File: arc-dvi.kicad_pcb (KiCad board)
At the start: 4 copper layers, 94.6 x 71.1 mm, 133 parts, among them J1 Conn_01x24_MountingPin, J2 VIDC Interposer, J3 SWD, J4 BOOT, J5 USB_B_Micro, J6 PWR, Q1 Q_NPN_BCE, U1 W25Q32JVSS, U2 RP2040, U3 ICE40HX4K-TQ144, U4 TDA19988BHN/C1,557, U5 LT1963AxST-3.3, U6 TLV70012_SOT23-5, U7 TLV70018_SOT23-5, Y1 12M 18pF

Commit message: v2: ADV7513 and FFC
Large work much progress - almost routed
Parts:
- removed FB6: FerriteBead_Small, Inductor_SMD:L_0603_1608Metric
- added C58: 0.1u, Capacitor_SMD:C_0603_1608Metric, F.Cu at (123.0, 93.0)
- added C59: 0.1u, Capacitor_SMD:C_0603_1608Metric, B.Cu at (124.8, 85.5)
- added D2: ESDA6V1BC6, Package_TO_SOT_SMD:SOT-23-6, F.Cu at (130.2, 67.2)
- added D3: D, Diode_SMD:D_0603_1608Metric, F.Cu at (124.0, 78.5)
- added D4: RCLAMP3328P, Package_DFN_QFN:UDFN-9_1.0x3.8mm_P0.5mm, F.Cu at (122.2, 70.8)
- added F1: 50mA, Fuse:Fuse_1206_3216Metric_Pad1.42x1.75mm_HandSolder, F.Cu at (131.2, 61.0)
- added J7: Misc, Connector_PinHeader_2.00mm:PinHeader_2x04_P2.00mm_Vertical, F.Cu at (74.0, 59.1)
- added J8: HDMI_A, Connector_HDMI:HDMI_A_Molex_208658-1001_Horizontal, F.Cu at (118.8, 57.0)
- added R18: 2K, Resistor_SMD:R_0603_1608Metric, B.Cu at (132.0, 76.5)
- added R19: 2K, Resistor_SMD:R_0603_1608Metric, B.Cu at (110.5, 73.8)
- added R20: 27K, Resistor_SMD:R_0603_1608Metric, F.Cu at (121.0, 77.8)
- added R21: 22, Resistor_SMD:R_0603_1608Metric, F.Cu at (110.8, 82.8)
- C34, C36, C37, C53, U5: moved to F.Cu
- C42: value 1u -> 10u
- C44: value 10u -> 0.1u; footprint Capacitor_SMD:C_0805_2012Metric -> Capacitor_SMD:C_0603_1608Metric
- C46: value 1u -> 0.1u
- C52: value 1u -> 0.1u; moved to F.Cu
- J1: value Conn_01x24_MountingPin -> Connector_50pin_FFC; footprint Connector_FFC-FPC:TE_2-1734839-4_1x24-1MP_P0.5mm_Horizontal -> Connector_FFC-FPC:Hirose_FH12-50S-0.5SH_1x50-1MP_P0.50mm_Horizontal
- J2: value VIDC Interposer -> 5V_IN; footprint Connector_PinHeader_2.54mm:PinHeader_2x25_P2.54mm_Vertical -> Connector_PinHeader_2.54mm:PinHeader_1x02_P2.54mm_Horizontal
- J6: value PWR -> PWR_USB; footprint Connector_PinHeader_2.54mm:PinHeader_1x03_P2.54mm_Vertical -> Connector_PinHeader_2.54mm:PinHeader_1x02_P2.54mm_Vertical
- R12, R13: value 10K -> 2K
- R14: value 10K, 1% -> 887, 1%
- R16: value 4k7 -> 4K7
- TP5: value AP4 -> SPD
- TP6: value AP3 -> P50
- TP7: value AP2 -> MCLK
- U4: value TDA19988BHN/C1,557 -> ADV7513BSWZ; footprint matt:QFN50P900X900X100-65N -> matt:QFP50P1200X1200X160-65N
- moved J1 80.9 mm to (80.0, 122.0), turned to 0 degrees
- moved TP1 80.2 mm to (56.2, 77.5)
- moved TP6 46.9 mm to (96.0, 119.2)
- moved C46 41.4 mm to (134.8, 79.5), turned to 90 degrees
- moved J4 39.3 mm to (71.5, 53.5)
- moved C34 37.6 mm to (56.8, 95.8), turned to 180 degrees
- moved FB1 31.8 mm to (61.8, 97.0), turned to -90 degrees
- moved C56 31.3 mm to (123.8, 79.3), turned to -90 degrees
- moved C42 30.6 mm to (136.8, 80.8), turned to 0 degrees
- moved C35 30.6 mm to (56.3, 86.7)
- moved C43 29.2 mm to (136.8, 82.8), turned to 0 degrees
- moved RN2 28.3 mm to (114.8, 88.8)
- moved TP7 28.3 mm to (139.5, 90.5)
- moved R14 27.7 mm to (140.5, 83.5), turned to 0 degrees
- moved RN1 27.4 mm to (114.8, 85.0)
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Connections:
- C42 pad 1: /Video/VDDA -> /Video/AVDD
- C43 pad 1: /Video/VDDA -> /Video/AVDD
- C44 pad 1: +1V8 -> /Video/AVDD
- C45 pad 1: /Video/VDDA_TX -> /Video/PVDD
- C46 pad 1: +1V8 -> /Video/AVDD
- C47 pad 1: /Video/VDDA_TX -> /Video/PVDD
- C48 pad 1: /Video/VDDA_PLL -> /Video/DVDD
- C50 pad 1: /Video/VDDA_PLL -> /Video/DVDD
- C52 pad 1: /Video/VDD_CORE -> /Video/PVDD
- C53 pad 1: /Video/VDD_CORE -> /Video/DVDD
- C54 pad 1: /Video/VDD_IO -> /Video/DVDD3
- C56 pad 1: /Video/VDD_IO -> /Video/DVDD3
- FB1 pad 2: /HOST_5V -> Net-(FB1-Pad2)
- FB3 pad 2: /Video/VDDA -> /Video/AVDD
- FB4 pad 2: /Video/VDDA_TX -> /Video/PVDD
- FB5 pad 2: /Video/VDDA_PLL -> /Video/DVDD
- FB7 pad 1: +1V8 -> +3V3
- FB7 pad 2: /Video/VDD_IO -> /Video/DVDD3
- J1 pad 1: VID_HPD -> VD0
- J1 pad 10: VID_CK+ -> VD8
- J1 pad 11: VID_D0- -> VD9
- J1 pad 12: GND -> VD10
- J1 pad 13: VID_D0+ -> VD11
- J1 pad 14: VID_D1- -> VD12
- J1 pad 15: GND -> VD13
- J1 pad 16: VID_D1+ -> GND
- J1 pad 17: VID_D2- -> VD14
- J1 pad 18: GND -> VD15
- J1 pad 19: VID_D2+ -> VD16
- J1 pad 2: +5V -> VD1
- J1 pad 20: CFG_SW3 -> VD17
- J1 pad 21: CFG_SW2 -> VD18
- J1 pad 22: CFG_SW1 -> VD19
- J1 pad 23: MCU_A2 -> VD20
- J1 pad 24: MCU_A1 -> GND
- J1 pad 3: GND -> VD2
- J1 pad 4: VID_DISP_SDA -> VD3
- J1 pad 5: VID_DISP_SCL -> VD4
- J1 pad 6: CFG_SW4 -> VD5
- J1 pad 7: VID_CEC -> VD6
- J1 pad 8: VID_CK- -> GND
- J1 pad 9: GND -> VD7
- J2 pad 1: VD15 -> Net-(FB1-Pad2)
- J2 pad 2: VD14 -> GND
- J6 pad 1: /VBUS -> +5V
- J6 pad 2: +5V -> /VBUS
- R12 pad 2: VID_DISP_SDA -> /Video/DDC_SDA
- R13 pad 2: VID_DISP_SCL -> /Video/DDC_SCL
- RN1 pad 1: RGB8 -> RGB23
- RN1 pad 2: RGB23 -> RGB22
- RN1 pad 3: RGB22 -> RGB21
- RN1 pad 4: RGB21 -> RGB20
- RN13 pad 1: ALT_VID_I2S_CLK -> ALT_VID_I2S_DATA
- RN13 pad 2: ALT_VID_I2S_WS -> ALT_VID_I2S_CLK
- RN13 pad 3: ALT_VID_I2S_DATA -> ALT_VID_I2S_WS
- RN13 pad 6: Net-(RN12-Pad8) -> Net-(RN12-Pad6)
- RN13 pad 7: Net-(RN12-Pad6) -> Net-(RN12-Pad7)
- RN13 pad 8: Net-(RN12-Pad7) -> Net-(RN12-Pad8)
- RN2 pad 1: RGB20 -> RGB19
- RN2 pad 2: RGB19 -> RGB18
- RN2 pad 3: RGB18 -> RGB17
- RN2 pad 4: RGB17 -> RGB16
- RN3 pad 1: VID_OUT_PCLK -> RGB11
- RN3 pad 2: RGB11 -> RGB10
- RN3 pad 3: RGB10 -> RGB9
- RN3 pad 4: RGB9 -> VID_OUT_PCLK
- RN3 pad 8: /Video/PCLK_R -> Net-(RN3-Pad8)
- RN4 pad 1: RGB16 -> RGB0
- RN4 pad 3: VID_OUT_VS -> VID_OUT_HS
- RN4 pad 4: VID_OUT_HS -> VID_OUT_VS
- RN4 pad 5: Net-(RN4-Pad5) -> Net-(U4-Pad2)
- RN4 pad 6: Net-(RN4-Pad6) -> Net-(U4-Pad64)
- RN4 pad 7: Net-(RN4-Pad7) -> Net-(U4-Pad63)
- RN4 pad 8: Net-(RN4-Pad8) -> Net-(U4-Pad62)
- RN5 pad 1: RGB3 -> RGB4
- RN5 pad 2: RGB2 -> RGB3
- RN5 pad 3: RGB1 -> RGB2
- RN5 pad 4: RGB0 -> RGB1
- RN6 pad 1: RGB7 -> RGB8
- RN6 pad 2: RGB6 -> RGB7
- RN6 pad 3: RGB5 -> RGB6
- RN6 pad 4: RGB4 -> RGB5
- TP6 pad 1: Net-(TP6-Pad1) -> Net-(J1-Pad50)
- U2 pad 31: CFG_SW4 -> MCU_VID_SDA
- U2 pad 32: CFG_SW3 -> MCU_VID_SCL
- U2 pad 36: MCU_A1 -> /MCU/spare24
- U2 pad 37: MCU_A2 -> /MCU/spare25
- U2 pad 38: CFG_SW2 -> /MCU/spare26
- U2 pad 39: CFG_SW1 -> /MCU/spare27
- U2 pad 40: MCU_VID_SDA -> /MCU/spare28
- U2 pad 41: MCU_VID_SCL -> ID_DET
- U3 pad 1: VID_OUT_HS -> VID_OUT_VS
- U3 pad 10: RGB20 -> RGB4
- U3 pad 101: VD30 -> VD23
- U3 pad 102: VD31 -> VD24
- U3 pad 104: VD0 -> VD25
- U3 pad 105: VD1 -> VD26
- U3 pad 106: VD2 -> VD27
- U3 pad 107: VD3 -> VD28
- U3 pad 11: RGB21 -> RGB5
- U3 pad 110: VD4 -> VD29
- U3 pad 112: VD5 -> VD30
- U3 pad 113: VD6 -> VD31
- U3 pad 114: VD7 -> VnVIDW
- U3 pad 115: VD8 -> VnHS
- U3 pad 116: VD9 -> VnVCS
- U3 pad 117: VD10 -> VnVIDRQ
- U3 pad 118: VD11 -> VnSNDRQ
- U3 pad 119: VD12 -> VFLYBK
- U3 pad 12: RGB22 -> RGB6
- U3 pad 120: VD13 -> VCKIN
- U3 pad 121: VD14 -> VVIDAK
- U3 pad 122: VD15 -> VSNDAK
- U3 pad 142: ALT_VID_I2S_DATA -> ALT_VID_I2S_WS
- U3 pad 143: ALT_VID_I2S_WS -> ALT_VID_I2S_CLK
- U3 pad 144: ALT_VID_I2S_CLK -> ALT_VID_I2S_DATA
- U3 pad 15: RGB23 -> RGB7
- U3 pad 17: RGB9 -> VID_OUT_PCLK
- U3 pad 18: RGB10 -> RGB9
- U3 pad 19: RGB11 -> RGB10
- U3 pad 2: VID_OUT_VS -> VID_OUT_HS
- U3 pad 20: VID_OUT_PCLK -> RGB11
- U3 pad 25: RGB0 -> RGB16
- U3 pad 26: RGB1 -> RGB17
- U3 pad 28: RGB2 -> RGB18
- U3 pad 29: RGB3 -> RGB19
- U3 pad 31: RGB4 -> RGB20
- U3 pad 32: RGB5 -> RGB21
- U3 pad 33: RGB6 -> RGB22
- U3 pad 34: RGB7 -> RGB23
- U3 pad 38: unconnected-(U3-Pad38) -> VID_CEC_CLK
- U3 pad 4: RGB16 -> RGB0
- U3 pad 7: RGB17 -> RGB1
- U3 pad 73: VVIDAK -> VD0
- U3 pad 74: VSNDAK -> VD1
- U3 pad 75: VFLYBK -> VD2
- U3 pad 76: VnSNDRQ -> VD3
- U3 pad 78: VnVIDRQ -> VD4
- U3 pad 79: VnHS -> VD5
- U3 pad 8: RGB18 -> RGB2
- U3 pad 80: VnVCS -> VD6
- U3 pad 81: VnVIDW -> VD7
- U3 pad 82: VD16 -> VD8
- U3 pad 83: VD17 -> VD9
- U3 pad 84: VD18 -> VD10
- U3 pad 85: VD19 -> VD11
- U3 pad 87: VD20 -> VD12
- U3 pad 88: VD21 -> VD13
- U3 pad 9: RGB19 -> RGB3
- U3 pad 90: VD22 -> VD14
- U3 pad 91: VD23 -> VD15
- U3 pad 93: VCKIN -> VD16
- U3 pad 94: VD24 -> VD17
- U3 pad 95: VD25 -> VD18
- U3 pad 96: VD26 -> VD19
- U3 pad 97: VD27 -> VD20
- U3 pad 98: VD28 -> VD21
- U3 pad 99: VD29 -> VD22
- U4 pad 1: Net-(RN7-Pad7) -> /Video/DVDD
- U4 pad 10: Net-(RN1-Pad7) -> Net-(RN12-Pad6)
- U4 pad 11: Net-(RN1-Pad6) -> /Video/DVDD
- U4 pad 12: Net-(RN1-Pad5) -> /Video/PVDD
- U4 pad 13: Net-(RN2-Pad8) -> /Video/PVDD
- U4 pad 14: /Video/VDD_IO -> Net-(R14-Pad1)
- U4 pad 15: Net-(RN2-Pad7) -> /Video/AVDD
- U4 pad 16: Net-(RN2-Pad6) -> /Video/HPD
- U4 pad 17: Net-(RN2-Pad5) -> /Video/TXC-
- U4 pad 18: Net-(RN4-Pad8) -> /Video/TXC+
- U4 pad 19: GND -> /Video/AVDD
- U4 pad 2: Net-(RN7-Pad6) -> Net-(U4-Pad2)
- U4 pad 20: Net-(RN4-Pad7) -> /Video/TX0-
- U4 pad 21: Net-(RN4-Pad6) -> /Video/TX0+
- U4 pad 22: Net-(RN4-Pad5) -> Net-(R18-Pad1)
- U4 pad 23: Net-(RN12-Pad7) -> /Video/TX1-
- U4 pad 24: Net-(RN12-Pad6) -> /Video/TX1+
- U4 pad 25: Net-(RN12-Pad8) -> /Video/AVDD
- U4 pad 26: Net-(TP7-Pad1) -> /Video/TX2-
- U4 pad 27: Net-(TP6-Pad1) -> /Video/TX2+
- U4 pad 28: Net-(TP5-Pad1) -> MCU_VID_IRQ
- U4 pad 29: /Video/VDD_CORE -> /Video/DVDD3
- U4 pad 3: Net-(RN7-Pad5) -> Net-(TP5-Pad1)
- U4 pad 30: VID_CEC -> /Video/CEC
- U4 pad 31: VID_HPD -> /Video/DVDD
- U4 pad 32: VID_DISP_SDA -> Net-(U4-Pad32)
- U4 pad 33: VID_DISP_SCL -> /Video/DDC_SCL
- U4 pad 34: Net-(R14-Pad1) -> /Video/DDC_SDA
- U4 pad 35: /Video/VDDA -> MCU_VID_SCL
- U4 pad 36: /Video/VDDA_TX -> MCU_VID_SDA
- U4 pad 37: VID_CK- -> Net-(RN1-Pad8)
- U4 pad 38: VID_CK+ -> Net-(RN1-Pad7)
- U4 pad 39: VID_D0- -> Net-(RN1-Pad6)
- U4 pad 4: /Video/PCLK_R -> Net-(TP7-Pad1)
- U4 pad 40: VID_D0+ -> Net-(RN1-Pad5)
- U4 pad 41: /Video/VDDA_TX -> Net-(RN2-Pad8)
- U4 pad 42: VID_D1- -> Net-(RN2-Pad7)
- U4 pad 43: VID_D1+ -> Net-(RN2-Pad6)
- U4 pad 44: VID_D2- -> Net-(RN2-Pad5)
- U4 pad 45: VID_D2+ -> Net-(RN7-Pad8)
- U4 pad 46: /Video/VDDA_TX -> Net-(RN7-Pad7)
- U4 pad 47: /Video/VDDA_PLL -> Net-(RN7-Pad6)
- U4 pad 48: /Video/VDDA_PLL -> Net-(RN7-Pad5)
- U4 pad 49: GND -> Net-(RN3-Pad8)
- U4 pad 5: /Video/VDD_CORE -> Net-(RN12-Pad8)
- U4 pad 50: MCU_VID_IRQ -> Net-(RN3-Pad7)
- U4 pad 51: MCU_VID_SDA -> /Video/DVDD
- U4 pad 52: MCU_VID_SCL -> Net-(RN3-Pad6)
- U4 pad 53: GND -> Net-(RN3-Pad5)
- U4 pad 54: GND -> Net-(RN6-Pad8)
- U4 pad 55: /Video/VDD_IO -> Net-(RN6-Pad7)
- U4 pad 56: Net-(RN6-Pad8) -> Net-(RN6-Pad6)
- U4 pad 57: Net-(RN6-Pad7) -> Net-(RN6-Pad5)
- U4 pad 58: Net-(RN6-Pad6) -> Net-(RN5-Pad8)
- U4 pad 59: Net-(RN6-Pad5) -> Net-(RN5-Pad7)
- U4 pad 6: Net-(RN3-Pad7) -> unconnected-(U4-Pad6)
- U4 pad 60: Net-(RN5-Pad8) -> Net-(RN5-Pad6)
- U4 pad 61: Net-(RN5-Pad7) -> Net-(RN5-Pad5)
- U4 pad 62: Net-(RN5-Pad6) -> Net-(U4-Pad62)
- U4 pad 63: Net-(RN5-Pad5) -> Net-(U4-Pad63)
- U4 pad 64: Net-(RN7-Pad8) -> Net-(U4-Pad64)
- U4 pad 7: Net-(RN3-Pad6) -> unconnected-(U4-Pad7)
- U4 pad 8: Net-(RN3-Pad5) -> unconnected-(U4-Pad8)
- U4 pad 9: Net-(RN1-Pad8) -> Net-(RN12-Pad7)
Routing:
- net GND: track 834.2 -> 566.2 mm, vias 85 -> 56
- net +5V: track 225.1 -> 47.8 mm
- net ID_DET: track 0.00 -> 94.3 mm, vias 0 -> 4
- net VID_CEC: track 76.9 -> 0.00 mm, vias 2 -> 0
- net VID_HPD: track 68.1 -> 0.00 mm
- net VID_DISP_SDA: track 64.7 -> 0.00 mm, vias 1 -> 0
- net VID_DISP_SCL: track 61.9 -> 0.00 mm, vias 1 -> 0
- net /Video/DVDD: track 0.00 -> 60.8 mm, vias 0 -> 4
- net VID_CK-: track 54.3 -> 0.00 mm
- net VID_CK+: track 54.3 -> 0.00 mm
- net VID_D0-: track 54.2 -> 0.00 mm
- net VID_D0+: track 54.2 -> 0.00 mm
- net VID_D2-: track 54.2 -> 0.00 mm
- net VID_D2+: track 54.2 -> 0.00 mm
- net VID_D1+: track 54.1 -> 0.00 mm
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- removed copper zone on In1.Cu, net +3V3
- removed copper zone on In2.Cu, net GND
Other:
- board size 94.6 x 71.1 mm -> 100 x 77 mm
- board text added: "Caution! Polarity! Check 3 times!"
- board text added: "Check values of C58 and friends, equal spread pls"
- board text added: "Gnd 5V"
- board text added: "USB boot ___"
- board text added: "___ Reset"
- board text added: "v2.0 190523 (c) 2023 Matt Evans"
- board text removed: "5"
- board text removed: "5B"
- board text removed: ">Reset"
- board text removed: ">USB boot"
- board text removed: "Digital out"
- board text removed: "^Pin 1"
- board text removed: "v1.0 180622 (c) 2022 Matt Evans"

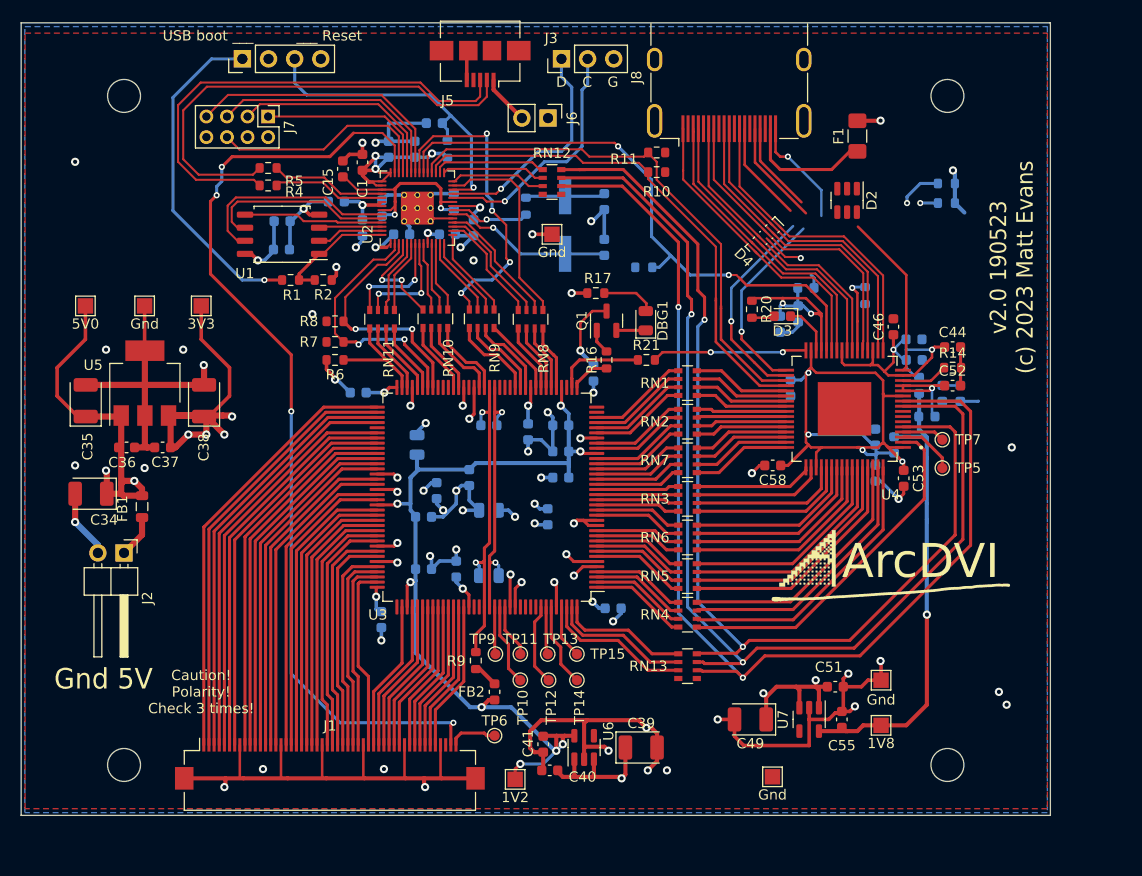
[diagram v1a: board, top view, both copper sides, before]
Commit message: 2.0 candiate: routed, looks neat, passes DRC
DVI differential pairs aren't tuned that nicely, but 'probs ok'
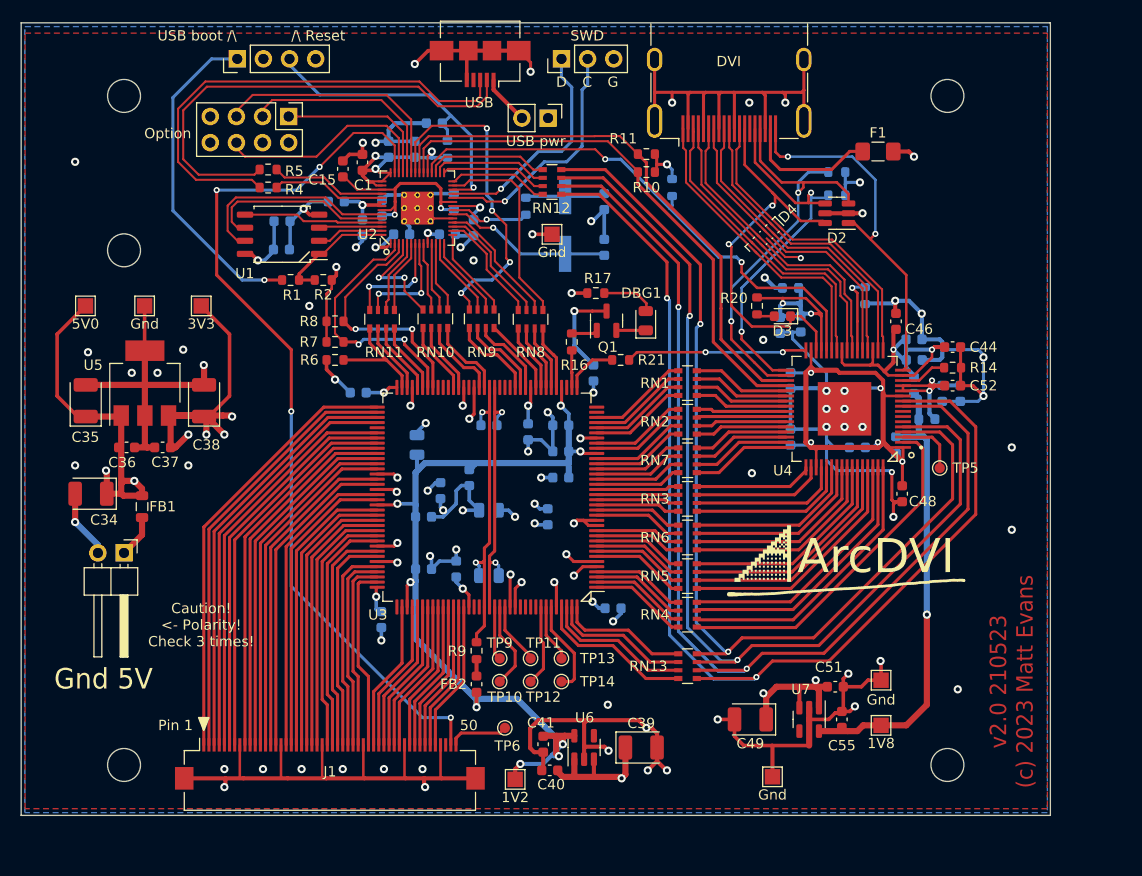
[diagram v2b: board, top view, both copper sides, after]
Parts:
- removed TP15: 219, TestPoint:TestPoint_Pad_D1.0mm
- removed TP7: MCLK, TestPoint:TestPoint_Pad_D1.0mm
- added H5: MountingHole, MountingHole:MountingHole_3.2mm_M3, F.Cu at (60.0, 72.1)
- C48: moved to F.Cu
- C53, C58: moved to B.Cu
- J7: footprint Connector_PinHeader_2.00mm:PinHeader_2x04_P2.00mm_Vertical -> Connector_PinHeader_2.54mm:PinHeader_2x04_P2.54mm_Vertical
- moved R12 11.1 mm to (129.2, 64.5)
- moved R13 10.7 mm to (129.2, 66.8)
- moved C53 8.84 mm to (132.0, 86.2)
- moved R19 8.22 mm to (113.2, 66.0), turned to -90 degrees
- moved C48 6.08 mm to (135.6, 95.8), turned to -90 degrees
- moved G*** 4.36 mm to (132.2, 103.2)
- moved R16 3.81 mm to (103.5, 81.0)
- moved C58 3.25 mm to (124.8, 90.2), turned to 90 degrees
- moved C50 3.05 mm to (131.2, 91.2), turned to 180 degrees
- moved F1 2.50 mm to (133.2, 62.5), turned to 0 degrees
- moved R21 2.50 mm to (108.2, 82.8)
- moved C54 2.08 mm to (123.8, 79.4)
- moved TP10 2.00 mm to (96.5, 114.0)
- moved C56 2.00 mm to (125.8, 79.2)
- moved J7 2.00 mm to (76.0, 59.1)
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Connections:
- D2 pad 3: /Video/DDC_SCL -> /Video/DDC_SDA
- D2 pad 4: /Video/DDC_SDA -> /Video/DDC_SCL
- J7 pad 7: /MCU/spare24 -> unconnected-(J7-Pad7)
- RN12 pad 1: VID_I2S_DATA -> VID_I2S_MCLK
- RN12 pad 2: VID_I2S_CLK -> VID_I2S_DATA
- RN12 pad 3: VID_I2S_WS -> VID_I2S_CLK
- RN12 pad 4: unconnected-(RN12-Pad4) -> VID_I2S_WS
- RN12 pad 5: unconnected-(RN12-Pad5) -> Net-(RN12-Pad5)
- RN13 pad 1: ALT_VID_I2S_DATA -> ALT_VID_I2S_MCLK
- RN13 pad 2: ALT_VID_I2S_CLK -> ALT_VID_I2S_DATA
- RN13 pad 3: ALT_VID_I2S_WS -> ALT_VID_I2S_CLK
- RN13 pad 4: unconnected-(RN13-Pad4) -> ALT_VID_I2S_WS
- RN13 pad 5: unconnected-(RN13-Pad5) -> Net-(RN12-Pad5)
- U2 pad 31: MCU_VID_SDA -> VID_I2S_MCLK
- U2 pad 32: MCU_VID_SCL -> MCU_VID_IRQ
- U2 pad 34: MCU_VID_IRQ -> MCU_VID_SDA
- U2 pad 35: FPGA_CLK -> MCU_VID_SCL
- U2 pad 36: /MCU/spare24 -> FPGA_CLK
- U3 pad 141: Net-(TP15-Pad1) -> ALT_VID_I2S_WS
- U3 pad 142: ALT_VID_I2S_WS -> ALT_VID_I2S_CLK
- U3 pad 143: ALT_VID_I2S_CLK -> ALT_VID_I2S_DATA
- U3 pad 144: ALT_VID_I2S_DATA -> ALT_VID_I2S_MCLK
- U3 pad 37: /FPGA/DBG_LED -> VID_CEC_CLK
- U3 pad 38: VID_CEC_CLK -> /FPGA/DBG_LED
- U4 pad 10: Net-(RN12-Pad6) -> Net-(RN12-Pad5)
- U4 pad 4: Net-(TP7-Pad1) -> Net-(RN12-Pad8)
- U4 pad 5: Net-(RN12-Pad8) -> Net-(RN12-Pad7)
- U4 pad 9: Net-(RN12-Pad7) -> Net-(RN12-Pad6)
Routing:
- net GND: track 566.2 -> 939.3 mm, vias 56 -> 81
- net +5V: track 47.8 -> 167.1 mm
- net Net-(RN12-Pad5): track 0.00 -> 109.9 mm, vias 0 -> 2
- net +3V3: track 404.1 -> 481.4 mm
- net /MCU/spare24: track 26.8 -> 0.00 mm
- net /Video/CEC: track 14.7 -> 39.4 mm, vias 0 -> 2
- net +1V1: track 0.00 -> 20.4 mm, vias 0 -> 2
- net ALT_VID_I2S_MCLK: track 0.00 -> 12.6 mm
- net /Video/DDC_SDA: track 30.8 -> 43.2 mm
- net VID_I2S_MCLK: track 0.00 -> 12.0 mm
- net /Video/HPD: track 26.8 -> 36.1 mm, vias 1 -> 2
- net /Video/DVDD: track 60.8 -> 52.3 mm, vias 4 -> 5
- net ID_DET: track 94.3 -> 87.7 mm
- net MCU_VID_IRQ: track 58.1 -> 52.0 mm
- net Net-(RN12-Pad7): track 107.4 -> 101.9 mm
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- added copper zone on In2.Cu, net +3V3
- added copper zone on In1.Cu, net GND
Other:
- board text added: "/\ Reset"
- board text added: "50"
- board text added: "Caution! <- Polarity! Check 3 times!"
- board text added: "DVI"
- board text added: "Option"
- board text added: "Pin 1"
- board text added: "SWD"
- board text added: "USB"
- board text added: "USB boot /\"
- board text added: "USB pwr"
- board text added: "v2.0 210523 (c) 2023 Matt Evans"
- board text removed: "Caution! Polarity! Check 3 times!"
- board text removed: "Check values of C58 and friends, equal spread pls"
- board text removed: "USB boot ___"
- board text removed: "___ Reset"
- board text removed: "v2.0 190523 (c) 2023 Matt Evans"

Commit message: Tuned pairs (better, at least)
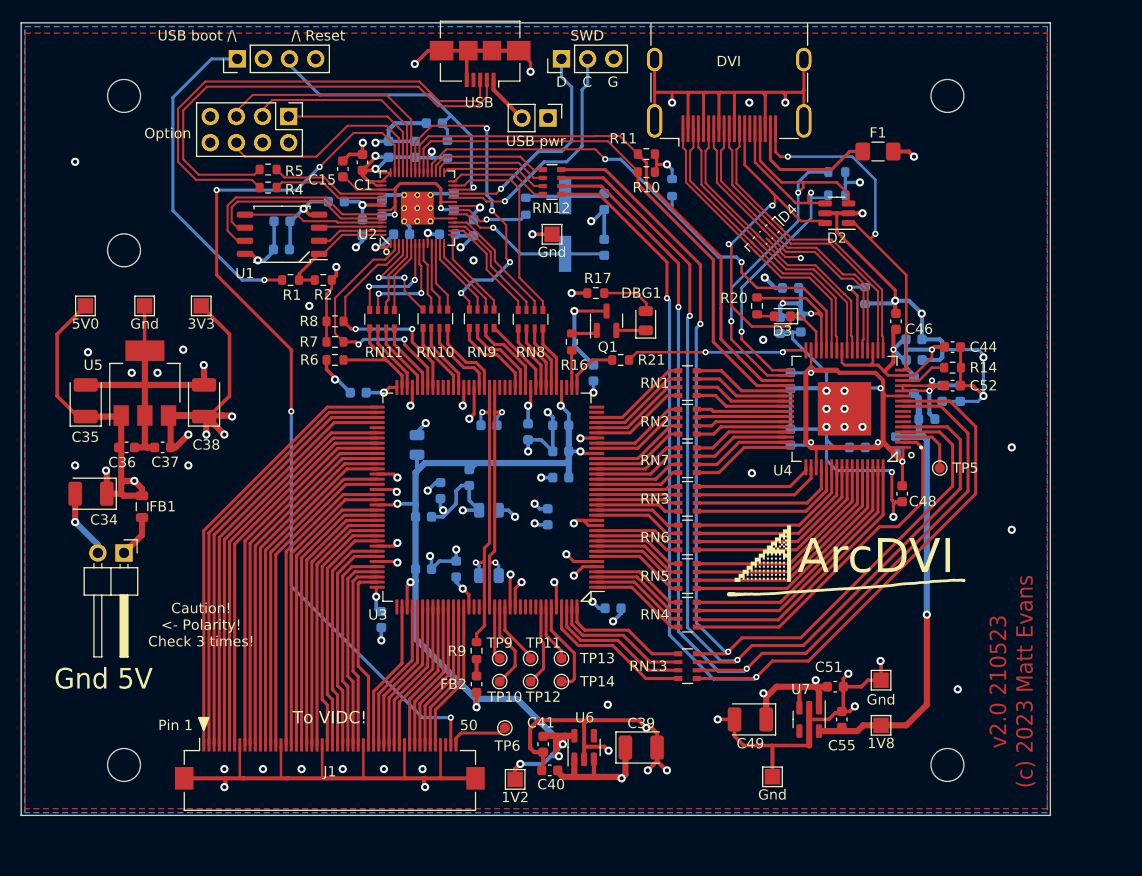
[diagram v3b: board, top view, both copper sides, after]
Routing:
- net GND: track 939.3 -> 950.2 mm
- net Net-(RN12-Pad5): track 109.9 -> 108.8 mm
- net Net-(RN12-Pad6): track 106.2 -> 105.2 mm
- net Net-(RN12-Pad7): track 101.9 -> 101.0 mm
- net Net-(RN4-Pad6): track 27.8 -> 27.0 mm
- net /Video/TX1-: track 30.0 -> 29.2 mm
- net /Video/TX1+: track 29.9 -> 29.1 mm
- net /Video/TX2-: track 30.0 -> 29.2 mm
- net /Video/TX2+: track 29.9 -> 29.1 mm
- net Net-(RN12-Pad8): track 98.2 -> 97.5 mm
- net Net-(RN4-Pad7): track 26.6 -> 25.9 mm
- net Net-(RN4-Pad8): track 25.5 -> 25.0 mm
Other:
- board text added: "To VIDC!"

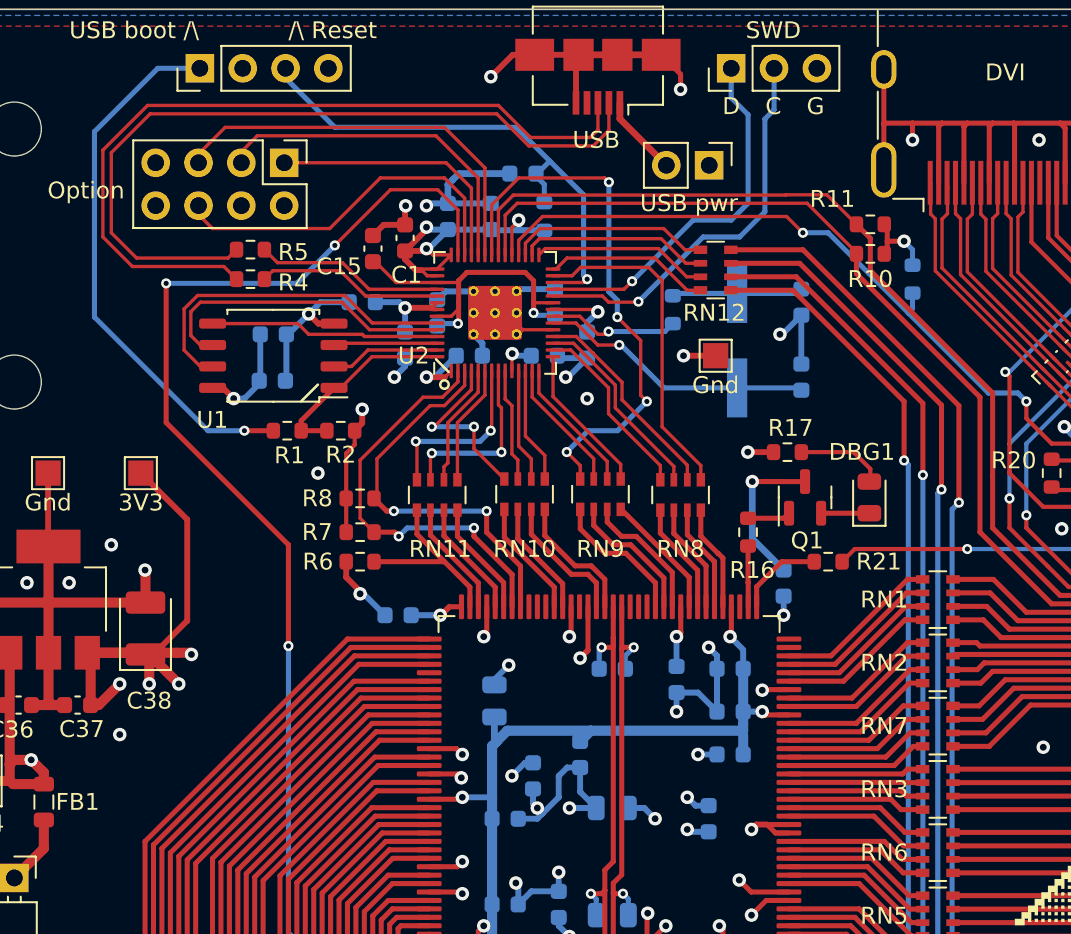
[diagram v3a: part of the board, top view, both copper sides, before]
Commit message: Tweaked layout, marked plcc centre
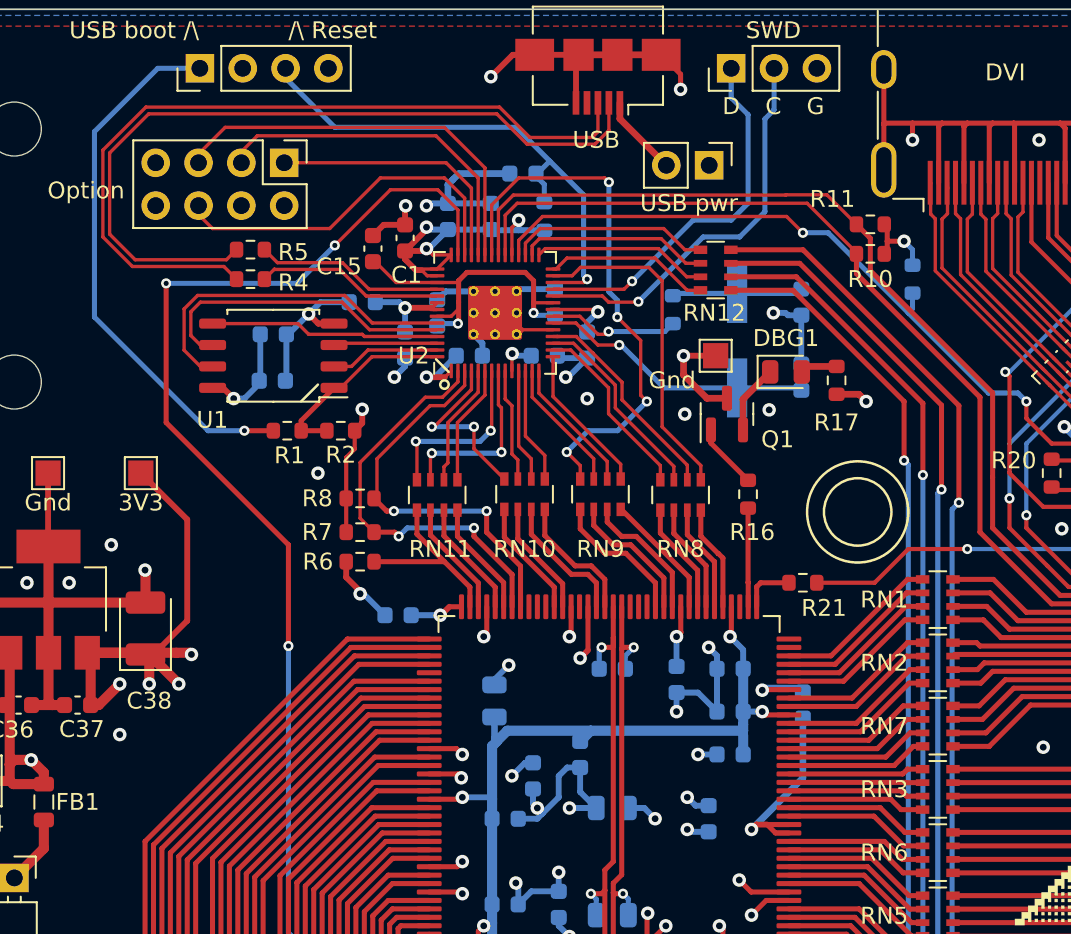
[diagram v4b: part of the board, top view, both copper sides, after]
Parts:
- moved D1 8.93 mm to (105.8, 71.5), turned to 0 degrees
- moved C21 7.32 mm to (106.8, 91.2), turned to -90 degrees
- moved Q1 6.77 mm to (102.2, 74.0)
- moved R17 5.16 mm to (108.8, 72.0), turned to 90 degrees
- moved R16 2.25 mm to (103.5, 78.8)
- moved R21 1.95 mm to (106.8, 84.0)
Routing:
- net GND: track 950.2 -> 964.2 mm, vias 81 -> 82
- net +3V3: track 481.4 -> 468.3 mm, vias 34 -> 33
- net Net-(D1-Pad2): track 5.28 -> 2.20 mm
- net /FPGA/DBG_LED: track 3.60 -> 5.85 mm
- net VID_CEC_CLK: track 5.21 -> 3.20 mm
- net Net-(R21-Pad2): track 17.6 -> 19.6 mm
- net Net-(Q1-Pad1): track 2.55 -> 3.90 mm
- net Net-(D1-Pad1): track 2.86 -> 4.11 mm
